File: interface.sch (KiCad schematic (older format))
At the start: 34 parts, among them P2 CONN_2, U10 SN74AUP1G00, U8 LT1618, U9 MAX9022

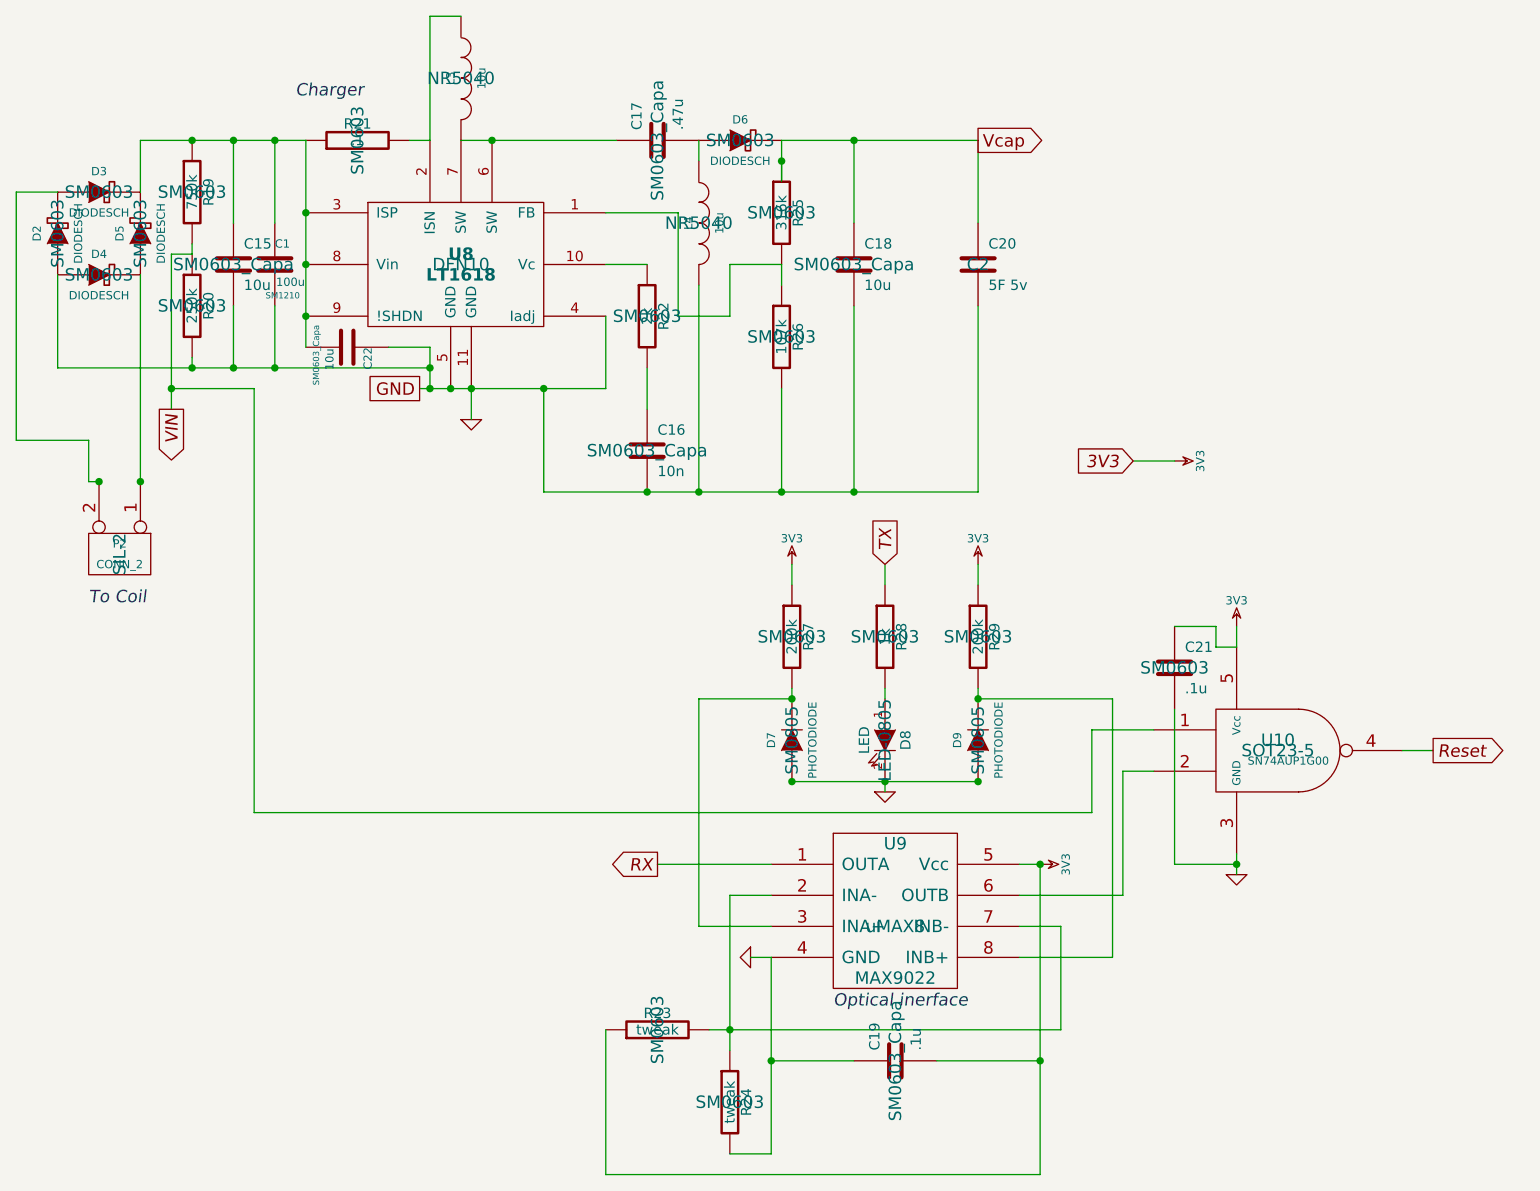
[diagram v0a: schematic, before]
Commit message: General layout/grounding tweaks, DC-DC layout improved, ADC set up for Vdd as ref, switchable 3v3_Analog for lower standby power, reset circuitry redone, Footprint fixes, better silkscreen.
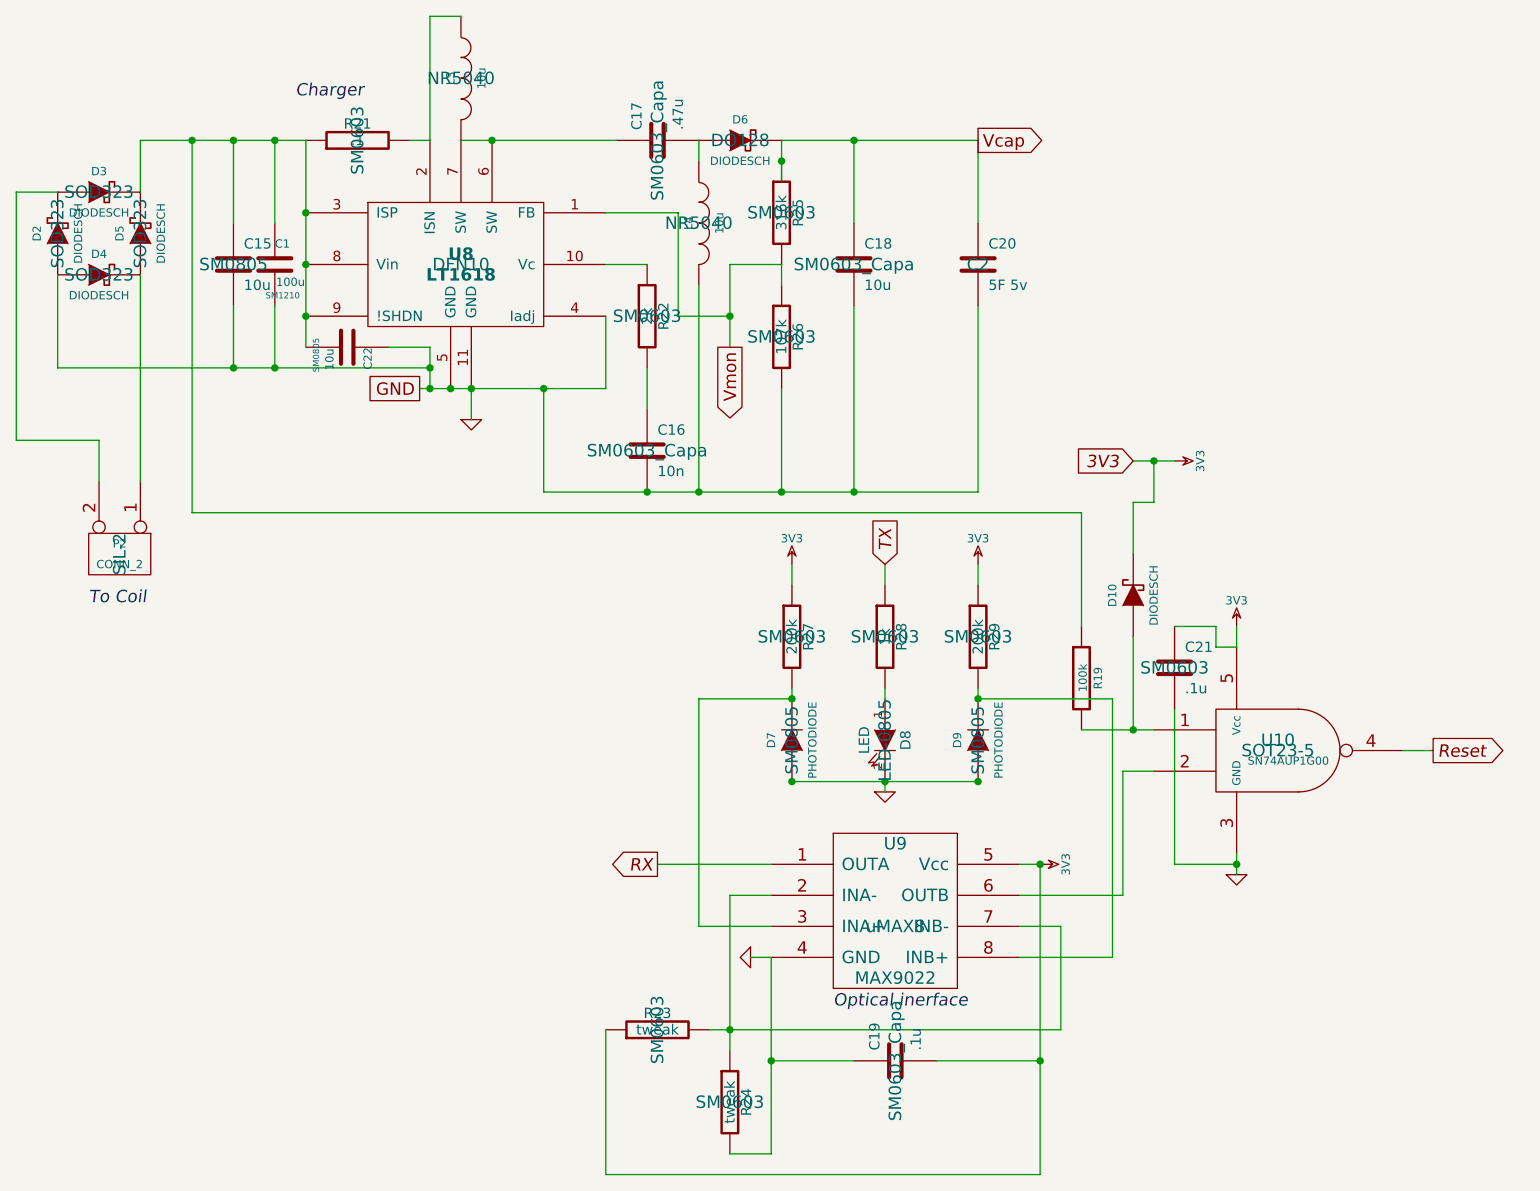
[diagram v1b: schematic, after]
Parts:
- removed R20: 250k, SM0603, symbol R
- added D10: DIODESCH, symbol DIODESCH
- C15, C22: footprint SM0603_Capa -> SM0805
- D2, D3, D4, D5: footprint SM0603 -> SOD323
- D6: footprint SM0603 -> DO128
- R19: value 750k -> 100k; footprint SM0603 -> (none)
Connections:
- net 3V3: now also D10.2 (K)
- net Vmon: now reaches R25.2, R26.1, U8.1 (FB)
- net VIN: no longer names the net of R19.2, U10.1
- net VIN: now also D10.1 (A)
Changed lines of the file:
@@
 $EndComp
 $Comp
-L GND #PWR023
+L GND #PWR021
 U 1 1 5122FAB8
 P 2800 2650
-F 0 "#PWR023" H 2800 2650 30  0001 C CNN
+F 0 "#PWR021" H 2800 2650 30  0001 C CNN
 F 1 "GND" H 2800 2580 30  0001 C CNN
 F 2 "" H 2800 2650 60  0001 C CNN
@@
 F 0 "C15" H 1700 2000 50  0000 L CNN
 F 1 "10u" H 1700 1800 50  0000 L CNN
-F 2 "SM0603_Capa" H 1650 1900 60  0000 C CNN
+F 2 "SM0805" H 1650 1900 60  0000 C CNN
 F 3 "" H 1650 1900 60  0001 C CNN
 	1    1650 1900
@@
 F 0 "D6" H 4100 1400 40  0000 C CNN
 F 1 "DIODESCH" H 4100 1200 40  0000 C CNN
-F 2 "SM0603" H 4100 1300 60  0000 C CNN
+F 2 "DO128" H 4100 1300 60  0000 C CNN
 F 3 "" H 4100 1300 60  0001 C CNN
 	1    4100 1300
@@
 F 0 "D3" H 1000 1650 40  0000 C CNN
 F 1 "DIODESCH" H 1000 1450 40  0000 C CNN
-F 2 "SM0603" H 1000 1550 60  0000 C CNN
+F 2 "SOD323" H 1000 1550 60  0000 C CNN
 F 3 "" H 1000 1550 60  0001 C CNN
 	1    1000 1550
@@
 F 0 "D5" H 1200 1850 40  0000 C CNN
 F 1 "DIODESCH" H 1200 1650 40  0000 C CNN
-F 2 "SM0603" H 1200 1750 60  0000 C CNN
+F 2 "SOD323" H 1200 1750 60  0000 C CNN
 F 3 "" H 1200 1750 60  0001 C CNN
 	1    1200 1750
@@
 F 0 "D4" H 1000 2050 40  0000 C CNN
 F 1 "DIODESCH" H 1000 1850 40  0000 C CNN
-F 2 "SM0603" H 1000 1950 60  0000 C CNN
+F 2 "SOD323" H 1000 1950 60  0000 C CNN
 F 3 "" H 1000 1950 60  0001 C CNN
 	1    1000 1950
@@
 F 0 "D2" H 800 1850 40  0000 C CNN
 F 1 "DIODESCH" H 800 1650 40  0000 C CNN
-F 2 "SM0603" H 800 1750 60  0000 C CNN
+F 2 "SOD323" H 800 1750 60  0000 C CNN
 F 3 "" H 800 1750 60  0001 C CNN
 	1    800  1750
@@
 $EndComp
 $Comp
-L R R19
-U 1 1 5123A8ED
-P 1450 1550
-F 0 "R19" V 1530 1550 50  0000 C CNN
-F 1 "750k" V 1450 1550 50  0000 C CNN
-F 2 "SM0603" H 1450 1550 60  0000 C CNN
-F 3 "" H 1450 1550 60  0001 C CNN
-	1    1450 1550
-	1    0    0    -1
-$EndComp
-$Comp
-L R R20
-U 1 1 5123A8FC
-P 1450 2100
-F 0 "R20" V 1530 2100 50  0000 C CNN
-F 1 "250k" V 1450 2100 50  0000 C CNN
-F 2 "SM0603" H 1450 2100 60  0000 C CNN
-F 3 "" H 1450 2100 60  0001 C CNN
-	1    1450 2100
-	1    0    0    -1
-$EndComp
-Text GLabel 1350 2600 3    60   Output Italic 0
-VIN
-$Comp
 L DIODE D9
 U 1 1 5123B3C5
@@
 $EndComp
 $Comp
-L GND #PWR024
+L GND #PWR022
 U 1 1 5123B3EA
 P 4800 4450
-F 0 "#PWR024" H 4800 4450 30  0001 C CNN
+F 0 "#PWR022" H 4800 4450 30  0001 C CNN
 F 1 "GND" H 4800 4380 30  0001 C CNN
 F 2 "" H 4800 4450 60  0001 C CNN
@@
 3V3
 $Comp
-L 3V3 #PWR025
+L 3V3 #PWR023
 U 1 1 5123B493
 P 6200 2850
-F 0 "#PWR025" H 6200 2950 40  0001 C CNN
+F 0 "#PWR023" H 6200 2950 40  0001 C CNN
 F 1 "3V3" H 6200 2975 40  0000 C CNN
 F 2 "" H 6200 2850 60  0001 C CNN
@@
 $EndComp
 $Comp
-L 3V3 #PWR026
+L 3V3 #PWR024
 U 1 1 5123B4E4
 P 5250 3350
-F 0 "#PWR026" H 5250 3450 40  0001 C CNN
+F 0 "#PWR024" H 5250 3450 40  0001 C CNN
 F 1 "3V3" H 5250 3475 40  0000 C CNN
 F 2 "" H 5250 3350 60  0001 C CNN
@@
 $EndComp
 $Comp
-L 3V3 #PWR027
+L 3V3 #PWR025
 U 1 1 5123B975
 P 4350 3350
-F 0 "#PWR027" H 4350 3450 40  0001 C CNN
+F 0 "#PWR025" H 4350 3450 40  0001 C CNN
 F 1 "3V3" H 4350 3475 40  0000 C CNN
 F 2 "" H 4350 3350 60  0001 C CNN
@@
 $EndComp
 $Comp
-L GND #PWR028
+L GND #PWR026
 U 1 1 5123FA46
 P 4150 5250
-F 0 "#PWR028" H 4150 5250 30  0001 C CNN
+F 0 "#PWR026" H 4150 5250 30  0001 C CNN
 F 1 "GND" H 4150 5180 30  0001 C CNN
 F 2 "" H 4150 5250 60  0001 C CNN
@@
 $EndComp
 $Comp
-L 3V3 #PWR029
+L 3V3 #PWR027
 U 1 1 5123FAB7
 P 5550 4800
-F 0 "#PWR029" H 5550 4900 40  0001 C CNN
+F 0 "#PWR027" H 5550 4900 40  0001 C CNN
 F 1 "3V3" H 5550 4925 40  0000 C CNN
 F 2 "" H 5550 4800 60  0001 C CNN
@@
 $EndComp
 $Comp
-L GND #PWR030
+L GND #PWR028
 U 1 1 5123FB1F
 P 6500 4850
-F 0 "#PWR030" H 6500 4850 30  0001 C CNN
+F 0 "#PWR028" H 6500 4850 30  0001 C CNN
 F 1 "GND" H 6500 4780 30  0001 C CNN
 F 2 "" H 6500 4850 60  0001 C CNN
@@
 $EndComp
 $Comp
-L 3V3 #PWR031
+L 3V3 #PWR029
 U 1 1 5123FB88
 P 6500 3650
-F 0 "#PWR031" H 6500 3750 40  0001 C CNN
+F 0 "#PWR029" H 6500 3750 40  0001 C CNN
 F 1 "3V3" H 6500 3775 40  0000 C CNN
 F 2 "" H 6500 3650 60  0001 C CNN
@@
 	4300 1900 4050 1900
 Wire Wire Line
-	4050 1900 4050 2150
+	4050 1900 4050 2300
 Wire Wire Line
 	4050 2150 3800 2150
@@
 	600  1550 600  2750
 Wire Wire Line
-	600  2750 950  2750
-Wire Wire Line
-	950  2750 950  2950
-Wire Wire Line
-	950  2950 1000 2950
-Connection ~ 1200 2950
-Connection ~ 1000 2950
-Connection ~ 1450 1300
-Wire Wire Line
-	1450 1850 1450 1800
-Wire Wire Line
-	1450 2350 1450 2400
-Connection ~ 1450 2400
-Wire Wire Line
-	1450 1850 1350 1850
-Wire Wire Line
-	1350 1850 1350 2600
-Wire Wire Line
 	5250 3950 5250 4000
 Wire Wire Line
@@
 	5950 4350 6100 4350
 Wire Wire Line
-	1350 2500 1750 2500
-Wire Wire Line
-	1750 2500 1750 4550
-Wire Wire Line
-	1750 4550 5800 4550
-Wire Wire Line
-	5800 4550 5800 4150
-Wire Wire Line
-	5800 4150 6100 4150
-Connection ~ 1350 2500
+	5750 4150 6100 4150
 Wire Wire Line
 	4150 5250 4250 5250
@@
 F 0 "C22" H 2200 2400 40  0000 L CNN
 F 1 "10u" H 2206 2215 40  0000 L CNN
-F 2 "SM0603_Capa" H 2238 2150 30  0000 C CNN
+F 2 "SM0805" H 2238 2150 30  0000 C CNN
 F 3 "~" H 2200 2300 60  0000 C CNN
 	1    2200 2300
@@
 	2400 2300 2600 2300
 Connection ~ 2600 2400
+$Comp
+L DIODESCH D10
+U 1 1 5254862B
+P 6000 3500
+F 0 "D10" H 6000 3600 40  0000 C CNN
+F 1 "DIODESCH" H 6000 3400 40  0000 C CNN
+F 2 "" H 6000 3500 60  0000 C CNN
+F 3 "" H 6000 3500 60  0000 C CNN
+	1    6000 3500
+	0    -1   -1   0
+$EndComp
+Wire Wire Line
+	6000 3700 6000 4150
+Connection ~ 6000 4150
+Wire Wire Line
+	6000 3300 6000 3050
+Wire Wire Line
+	6000 3050 6100 3050
+Wire Wire Line
+	6100 3050 6100 2850
+Connection ~ 6100 2850
+$Comp
+L R R19
+U 1 1 525487CC
+P 5750 3900
+F 0 "R19" V 5830 3900 40  0000 C CNN
+F 1 "100k" V 5757 3901 40  0000 C CNN
+F 2 "" V 5680 3900 30  0000 C CNN
+F 3 "" H 5750 3900 30  0000 C CNN
+	1    5750 3900
+	1    0    0    -1
+$EndComp
+Wire Wire Line
+	5750 3100 5750 3650
+Wire Wire Line
+	1450 3100 5750 3100
+Wire Wire Line
+	1000 2950 1000 2750
+Wire Wire Line
+	1000 2750 600  2750
+Text GLabel 4050 2300 3    60   Output ~ 0
+Vmon
+Connection ~ 4050 2150
+Wire Wire Line
+	1450 1300 1450 3100
+Connection ~ 1450 1300
 $EndSCHEMATC
